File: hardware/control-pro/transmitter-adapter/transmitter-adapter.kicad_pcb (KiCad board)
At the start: 2 copper layers, 68.6 x 53.3 mm, 4 parts, among them J3 IO EXTENSION

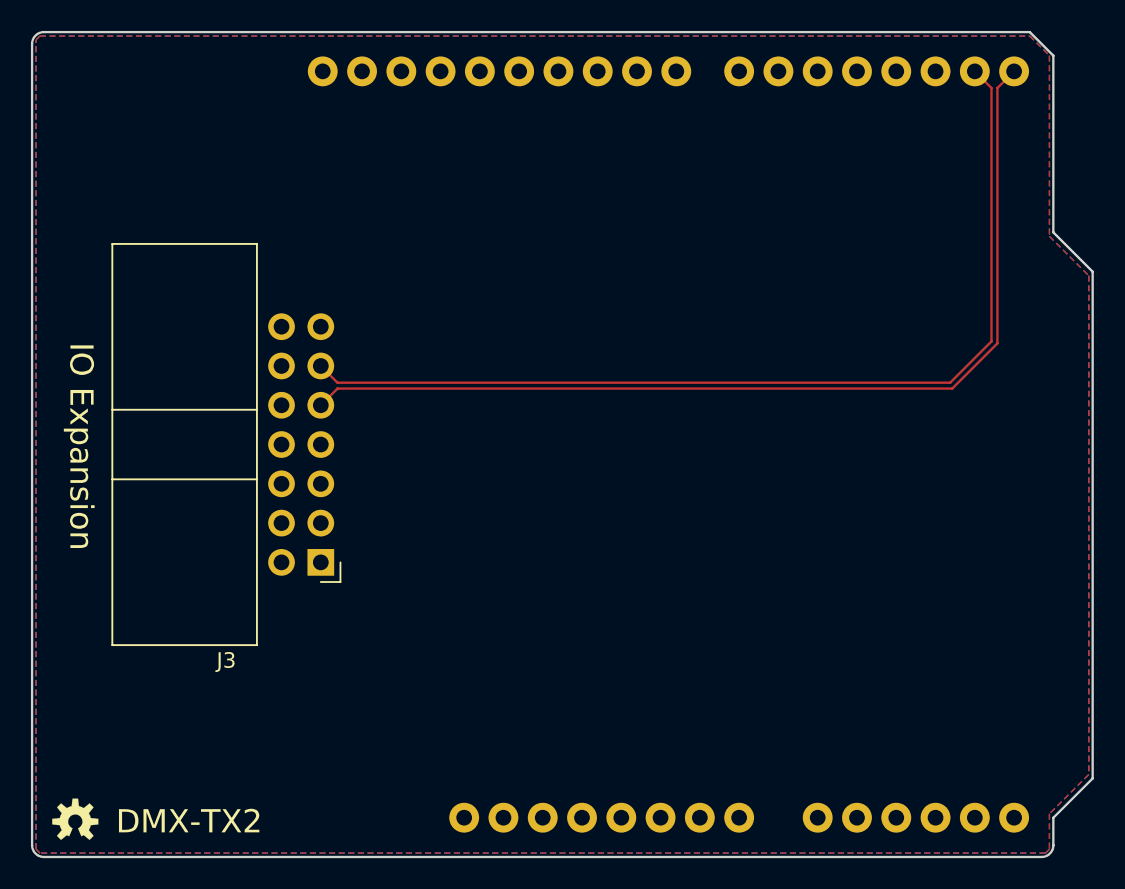
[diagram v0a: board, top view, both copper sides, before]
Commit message: Users/sparky/dmxio1 rev1 7 (#28)
* Add DMX-IO1, DMX-512 support
- Added termination switch
- Change to RFM-0505S
- Change to MAX485E
- Swap A and B on Max485
- Avoid split power planes under WH4
- Remove pads from XLR alignment pins
- Fix pinout of U1
- Added io-dmx module Receiver software
- Added io-dmx module Transmitter software
- Breakup TX2 into 2 boards, allowing IO boards to be used with TX1.
- Update PCB links in readme, bom, parts
- Update U1 part links in readme
- Added termination switch
- Change to RFM-0505S
- Change to MAX485E
- Swap A and B on Max485
- Avoid split power planes under WH4
- Remove pads from XLR alignment pins
- Update readme
- Add IO1 parts to BOM generation.

* Put text on Back Silk instead of Front Mask.

* Update board link.
Mark as verified.

* Add serial output for DMX mode.

* Remove #if for DMX-512 support.
Mark verified.
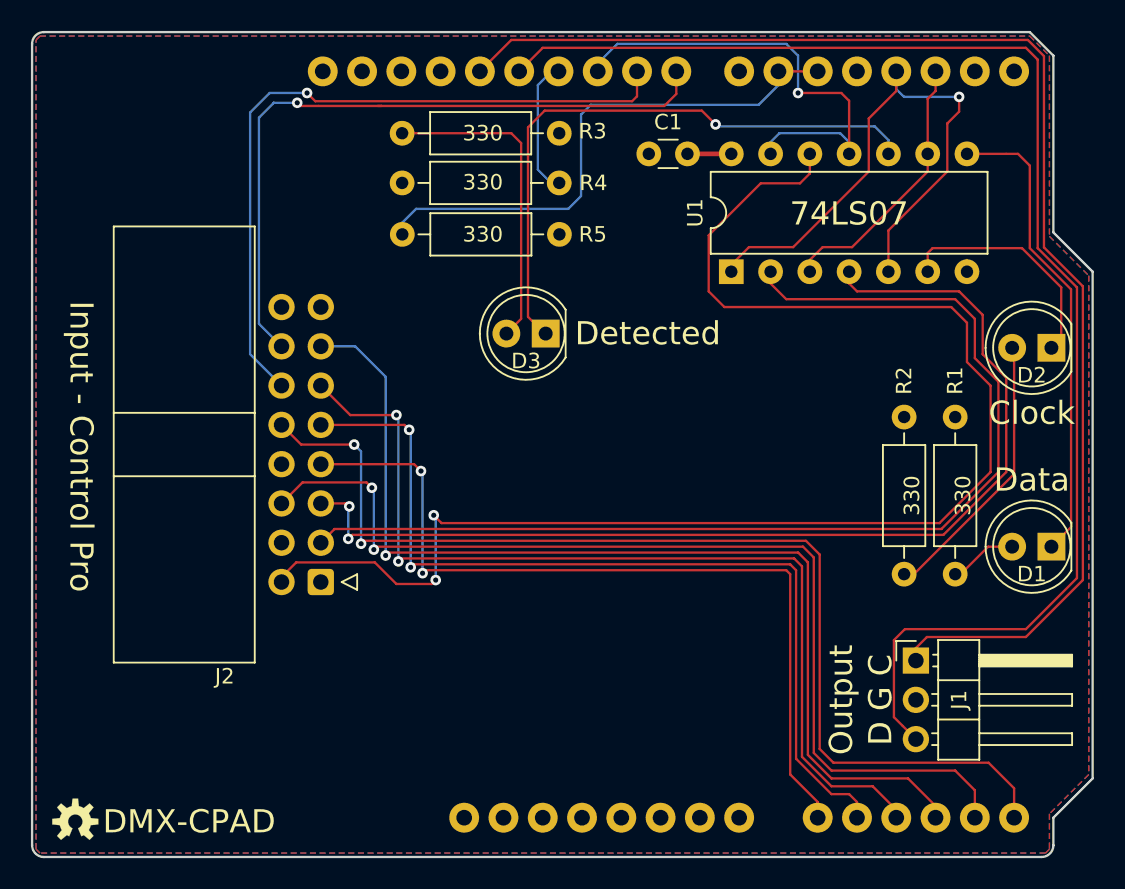
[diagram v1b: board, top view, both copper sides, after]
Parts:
- removed J3: IO EXTENSION, Connector_IDC:IDC-Header_2x07_P2.54mm_Horizontal
- added C1: 0.1uF, Capacitor_THT:C_Disc_D3.0mm_W1.6mm_P2.50mm, F.Cu at (156.2, 71.1)
- added D1: DATA, LED_THT:LED_D5.0mm, F.Cu at (182.2, 96.5)
- added D2: CLOCK, LED_THT:LED_D5.0mm, F.Cu at (182.2, 83.7)
- added D3: DETECTED, LED_THT:LED_D5.0mm, F.Cu at (149.5, 82.7)
- added J1: Output, Connector_PinHeader_2.54mm:PinHeader_1x03_P2.54mm_Horizontal, F.Cu at (173.5, 103.9)
- added J2: INPUT, Connector_IDC:IDC-Header_2x08_P2.54mm_Horizontal, F.Cu at (135.0, 98.8)
- added R1: 330, Resistor_THT:R_Axial_DIN0207_L6.3mm_D2.5mm_P10.16mm_Horizontal, F.Cu at (176.0, 88.1)
- added R2: 330, Resistor_THT:R_Axial_DIN0207_L6.3mm_D2.5mm_P10.16mm_Horizontal, F.Cu at (172.7, 88.1)
- added R3: 330, Resistor_THT:R_Axial_DIN0207_L6.3mm_D2.5mm_P10.16mm_Horizontal, F.Cu at (150.4, 69.8)
- added R4: 330, Resistor_THT:R_Axial_DIN0207_L6.3mm_D2.5mm_P10.16mm_Horizontal, F.Cu at (150.4, 73.0)
- added R5: 330, Resistor_THT:R_Axial_DIN0207_L6.3mm_D2.5mm_P10.16mm_Horizontal, F.Cu at (150.4, 76.3)
- added U1: 74LS07, Package_DIP:DIP-14_W7.62mm, F.Cu at (161.5, 78.7)
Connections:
- A1 pad 10: Net-(A1-Pad10) -> /A1
- A1 pad 11: Net-(A1-Pad11) -> /A2
- A1 pad 12: Net-(A1-Pad12) -> /A3
- A1 pad 13: Net-(A1-Pad13) -> /A4
- A1 pad 14: Net-(A1-Pad14) -> /A5
- A1 pad 15: /DMX-RX -> Net-(A1-Pad15)
- A1 pad 16: /DMX-TX -> Net-(A1-Pad16)
- A1 pad 17: Net-(A1-Pad17) -> /~DATA_OUT
- A1 pad 18: Net-(A1-Pad18) -> /~CLOCK_OUT
- A1 pad 21: Net-(A1-Pad21) -> Net-(A1-Pad20)
- A1 pad 23: Net-(A1-Pad23) -> /~CLK_FST
- A1 pad 24: Net-(A1-Pad24) -> /~CLK_SLO
- A1 pad 25: Net-(A1-Pad25) -> /~HWD_DT_OUT
- A1 pad 27: Net-(A1-Pad27) -> /RX
- A1 pad 28: Net-(A1-Pad28) -> /RXCLK
- A1 pad 9: Net-(A1-Pad9) -> /A0
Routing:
- net /~HWD_DT: track 0.00 -> 94.1 mm, vias 0 -> 2
- net /RX: track 0.00 -> 89.5 mm
- net /RXCLK: track 0.00 -> 86.7 mm
- net /A5: track 0.00 -> 71.6 mm, vias 0 -> 2
- net /~CLOCK: track 0.00 -> 71.2 mm
- net /~DATA: track 0.00 -> 69.4 mm, vias 0 -> 2
- net /A3: track 0.00 -> 67.0 mm, vias 0 -> 1
- net /A4: track 0.00 -> 65.3 mm, vias 0 -> 2
- net /DMX-RX: track 63.4 -> 0.00 mm
- net /DMX-TX: track 62.8 -> 0.00 mm
- net /A2: track 0.00 -> 61.9 mm, vias 0 -> 2
- net /A1: track 0.00 -> 58.2 mm, vias 0 -> 2
- net /A0: track 0.00 -> 53.7 mm, vias 0 -> 2
- net /~CLK_SLO: track 0.00 -> 46.0 mm, vias 0 -> 1
- net /~CLK_FST: track 0.00 -> 44.9 mm, vias 0 -> 1
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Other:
- board text added: "74LS07"
- board text added: "Clock"
- board text added: "D G C"
- board text added: "DMX-CPAD"
- board text added: "DMX-CPAD, Rev 1.3 Sparky Bobo Designs"
- board text added: "Data"
- board text added: "Detected"
- board text added: "Input - Control Pro"
- board text added: "Output"
- board text removed: "DMX-TX2"
- board text removed: "DMX-TX2, Rev 1.4 Sparky Bobo Designs"
- board text removed: "IO Expansion"
